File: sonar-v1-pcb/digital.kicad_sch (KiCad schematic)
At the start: 28 parts, among them J40 DIP-48 socket - Cmod A7-35T, J41 FT232H breakout header (Adafr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, J42 PDM array header / Pico 2 rib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, J43 HR911105A MagJack, J44 SJ1 DNP: Cmod 3V3 <> board +3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, J45 SJ2 DNP: Cmod VU <> board 5V, U50 LAN8720A, X1 50 MHz (DNP)

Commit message: T-011 audit: PASS all areas; fix LAN8720A refdes U50->U60 collision; regenerate sheet/pinmap/XDC
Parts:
- removed U50: LAN8720A, Package_DFN_QFN:QFN-24-1EP_4x4mm_P0.5mm_EP2.5x2.5mm, symbol Interface_Ethernet:LAN8720A
- added U60: LAN8720A, Package_DFN_QFN:QFN-24-1EP_4x4mm_P0.5mm_EP2.5x2.5mm, symbol Interface_Ethernet:LAN8720A
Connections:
- net +3.3V: now also U60.1 (VDD2A), U60.19 (VDD1A), U60.9 (VDDIO)
- net ETH_CRS_DV: now also U60.11 (CRS_DV/MODE2)
- net ETH_INTSEL: now also U60.2 (LED2/~{INTSEL})
- net ETH_MDC: now also U60.13 (MDC)
- net ETH_MDIO: now also U60.12 (MDIO)
- net ETH_RBIAS: now also U60.24 (RBIAS)
- net ETH_REF_CLK: now also U60.5 (XTAL1/CLKIN)
- net ETH_REGOFF: now also U60.3 (LED1/REGOFF)
- net ETH_RST_N: now also U60.15 (~{RST})
- net ETH_RXD0: now also U60.8 (RXD0/MODE0)
- net ETH_RXD1: now also U60.7 (RXD1/MODE1)
- net ETH_RXN: now also U60.22 (RXN)
- net ETH_RXP: now also U60.23 (RXP)
- net ETH_RX_ER: now also U60.10 (RXER/PHYAD0)
- net ETH_TXD0: now also U60.17 (TXD0)
- net ETH_TXD1: now also U60.18 (TXD1)
- net ETH_TXN: now also U60.20 (TXN)
- net ETH_TXP: now also U60.21 (TXP)
- net ETH_TX_EN: now also U60.16 (TXEN)
- net ETH_VDDCR: now also U60.6 (VDDCR)
- net GND: now also U60.25 (VSS)
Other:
- note added: "AUTHORITATIVE PIN TABLE: orchestration/pinmap.md (generated by scripts/gen_digital_sheet.py). Clock-capable pins: PDM_CLK_FB=pio36 (MRCC), FT_CLKOUT=pio43 (SRCC), ETH_REF_CLK=pio3 (MRCC) - all double-sourced. Package pins: offline transcription of the Digilent Cmod-A7-Master.xdc, audited offline by a second agent 2026-08-26; live master-XDC diff still required before T-020 synthesis (see orchestr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"
- note added: "DNP ETHERNET PROVISION (D012 amendment b): U60 LAN8720A + J43 HR911105A MagJack + X1 50 MHz osc + R400-R403/C400-C406 are ALL DNP on v1. 100M RMII carries only the decimated stream (raw PDM needs the FT232H). Populate-and-learn milestone, never a respin. MODE[2:0]/PHYAD0 strap levels (RXD0/RXD1/CRS_DV/RXER pins) are sampled at nRST release - Artix-7 config-time weak pull-ups can override the PHY'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"
- note removed: "AUTHORITATIVE PIN TABLE: orchestration/pinmap.md (generated by scripts/gen_digital_sheet.py). Clock-capable pins: PDM_CLK_FB=pio36 (MRCC), FT_CLKOUT=pio43 (SRCC), ETH_REF_CLK=pio3 (MRCC) - all double-sourced. Package pins are offline transcriptions of the Digilent Cmod-A7-Master.xdc - audit against the live master XDC before T-020 synthesis."
- note removed: "DNP ETHERNET PROVISION (D012 amendment b): U50 LAN8720A + J43 HR911105A MagJack + X1 50 MHz osc + R400-R403/C400-C406 are ALL DNP on v1. 100M RMII carries only the decimated stream (raw PDM needs the FT232H). Populate-and-learn milestone, never a respin. MODE[2:0]/PHYAD0 strap levels (RXD0/RXD1/CRS_DV/RXER pins) are sampled at nRST release - Artix-7 config-time weak pull-ups can override the PHY'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"
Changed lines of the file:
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@@
 		)
 	)
-	(text "AUTHORITATIVE PIN TABLE: orchestration/pinmap.md (generated by scripts/gen_digital_sheet.py).\nClock-capable pins: PDM_CLK_FB=pio36 (MRCC), FT_CLKOUT=pio43 (SRCC), ETH_REF_CLK=pio3 (MRCC) - all double-sourced.\nPackage pins are offline transcriptions of the Digilent Cmod-A7-Master.xdc - audit against the live master XDC before T-020 synthesis."
+	(text "AUTHORITATIVE PIN TABLE: orchestration/pinmap.md (generated by scripts/gen_digital_sheet.py).\nClock-capable pins: PDM_CLK_FB=pio36 (MRCC), FT_CLKOUT=pio43 (SRCC), ETH_REF_CLK=pio3 (MRCC) - all double-sourced.\nPackage pins: offline transcription of the Digilent Cmod-A7-Master.xdc, audited offline by a second agent 2026-08-26;\nlive master-XDC diff still required before T-020 synthesis (see orchestration/pinmap.md)."
 		(exclude_from_sim no)
 		(at 25.4 18.5 0)
@@
 		)
 	)
-	(text "DNP ETHERNET PROVISION (D012 amendment b): U50 LAN8720A + J43 HR911105A MagJack + X1 50 MHz osc + R400-R403/C400-C406 are ALL DNP on v1.\n100M RMII carries only the decimated stream (raw PDM needs the FT232H). Populate-and-learn milestone, never a respin.\nMODE[2:0]/PHYAD0 strap levels (RXD0/RXD1/CRS_DV/RXER pins) are sampled at nRST release - Artix-7 config-time weak pull-ups can\noverride the PHY's internal strap pulls; determine strap resistors from the LAN8720A datasheet at populate time.\nTCT to +3.3V / RCT decoupled per LAN8720A voltage-mode reference - verify against the chosen PHY+jack datasheets at populate."
+	(text "DNP ETHERNET PROVISION (D012 amendment b): U60 LAN8720A + J43 HR911105A MagJack + X1 50 MHz osc + R400-R403/C400-C406 are ALL DNP on v1.\n100M RMII carries only the decimated stream (raw PDM needs the FT232H). Populate-and-learn milestone, never a respin.\nMODE[2:0]/PHYAD0 strap levels (RXD0/RXD1/CRS_DV/RXER pins) are sampled at nRST release - Artix-7 config-time weak pull-ups can\noverride the PHY's internal strap pulls; determine strap resistors from the LAN8720A datasheet at populate time.\nTCT to +3.3V / RCT decoupled per LAN8720A voltage-mode reference - verify against the chosen PHY+jack datasheets at populate."
 		(exclude_from_sim no)
 		(at 285 25 0)
@@
 		(dnp yes)
 		(fields_autoplaced yes)
-		(property "Reference" "U50"
+		(property "Reference" "U60"
 			(at 340.36 111.76 0)
 			(show_name no)
@@
 			(project "sonar"
 				(path "/f72ceae0-eee4-4385-b0e8-639846bcb5f2/d19a7a11-b1c2-4d3e-8f40-a11d1a11ce11"
-					(reference "U50")
+					(reference "U60")
 					(unit 1)
 				)

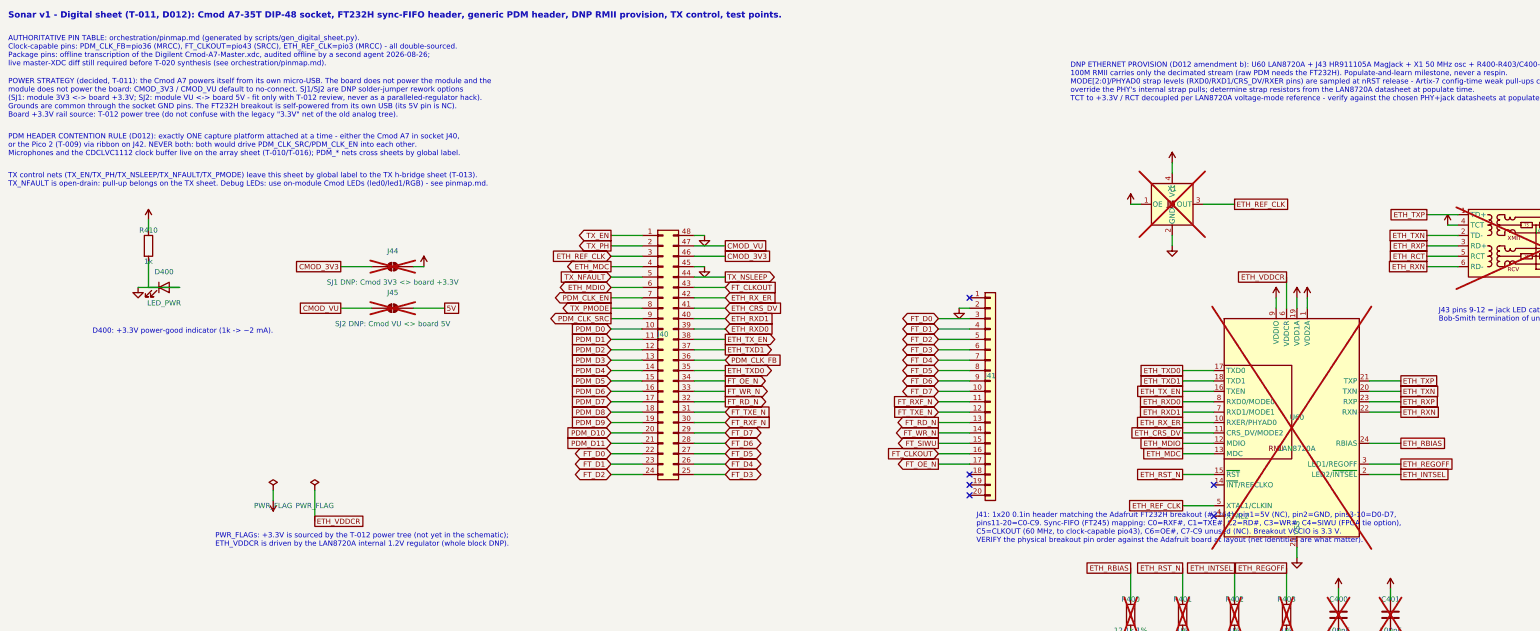
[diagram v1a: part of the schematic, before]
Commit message: T-011 repair: true DIP positions (skip 15/16 analog, 24=VU 25=GND); live-XDC check script; revert CC list to true labels
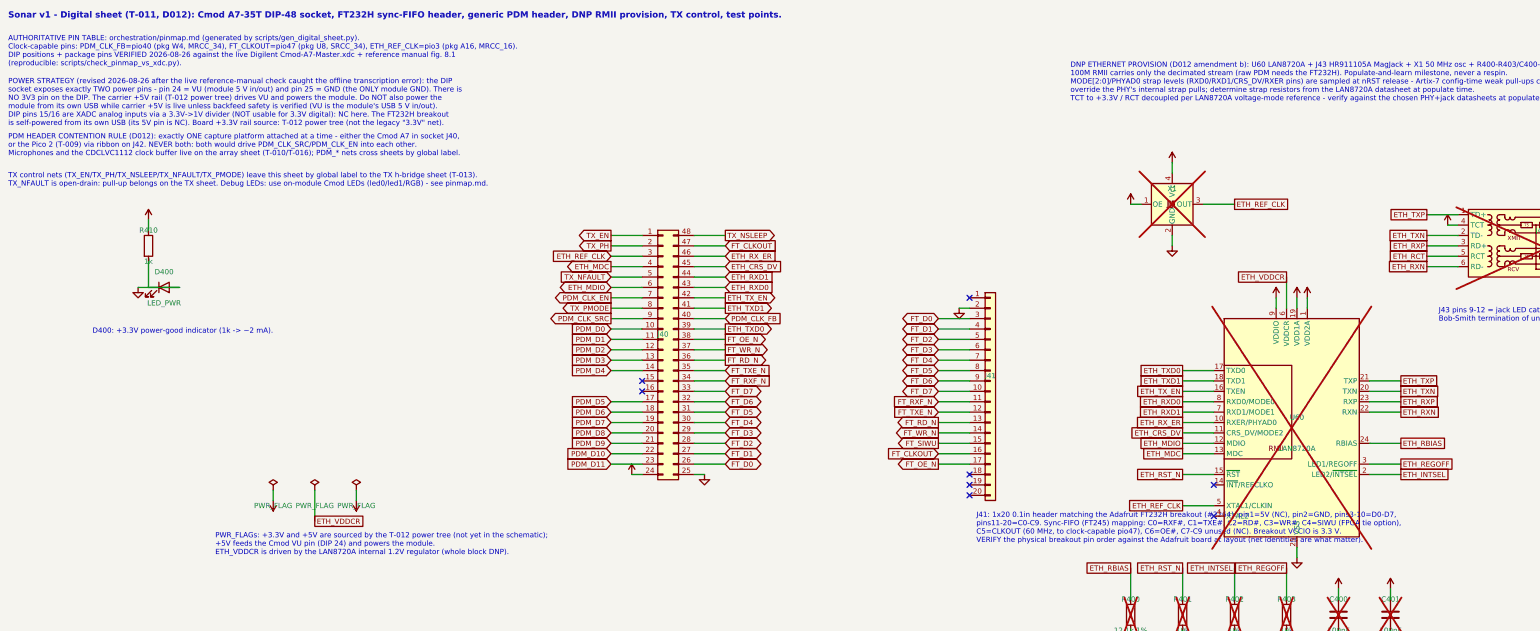
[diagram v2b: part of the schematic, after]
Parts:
- removed J44: SJ1 DNP: Cmod 3V3 <> board +3.3V, Jumper:SolderJumper-2_P1.3mm_Open_RoundedPad1.0x1.5mm, symbol Jumper:SolderJumper_2_Open
- removed J45: SJ2 DNP: Cmod VU <> board 5V, Jumper:SolderJumper-2_P1.3mm_Open_RoundedPad1.0x1.5mm, symbol Jumper:SolderJumper_2_Open
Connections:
- net CMOD_3V3 is gone; now on net ETH_RX_ER: J40.46 (Pin_46)
- net CMOD_VU is gone; now on net FT_CLKOUT: J40.47 (Pin_47)
- net ETH_CRS_DV: now also J40.45 (Pin_45); no longer J40.41 (Pin_41)
- net ETH_RXD0: now also J40.43 (Pin_43); no longer J40.39 (Pin_39)
- net ETH_RXD1: now also J40.44 (Pin_44); no longer J40.40 (Pin_40)
- net ETH_RX_ER: no longer J40.42 (Pin_42)
- net ETH_TXD0: now also J40.39 (Pin_39); no longer J40.35 (Pin_35)
- net ETH_TXD1: now also J40.41 (Pin_41); no longer J40.37 (Pin_37)
- net ETH_TX_EN: now also J40.42 (Pin_42); no longer J40.38 (Pin_38)
- net FT_CLKOUT: no longer J40.43 (Pin_43)
- net FT_D0: now also J40.26 (Pin_26); no longer J40.22 (Pin_22)
- net FT_D1: now also J40.27 (Pin_27); no longer J40.23 (Pin_23)
- net FT_D2: now also J40.28 (Pin_28); no longer J40.24 (Pin_24)
- net FT_D3: now also J40.29 (Pin_29); no longer J40.25 (Pin_25)
- net FT_D4: now also J40.30 (Pin_30); no longer J40.26 (Pin_26)
- net FT_D5: now also J40.31 (Pin_31); no longer J40.27 (Pin_27)
- net FT_D6: now also J40.32 (Pin_32); no longer J40.28 (Pin_28)
- net FT_D7: now also J40.33 (Pin_33); no longer J40.29 (Pin_29)
- net FT_OE_N: now also J40.38 (Pin_38); no longer J40.34 (Pin_34)
- net FT_RD_N: now also J40.36 (Pin_36); no longer J40.32 (Pin_32)
- net FT_RXF_N: now also J40.34 (Pin_34); no longer J40.30 (Pin_30)
- net FT_TXE_N: now also J40.35 (Pin_35); no longer J40.31 (Pin_31)
- net FT_WR_N: now also J40.37 (Pin_37); no longer J40.33 (Pin_33)
- net GND: now also J40.25 (Pin_25); no longer J40.45 (Pin_45), J40.48 (Pin_48)
- net PDM_CLK_FB: now also J40.40 (Pin_40); no longer J40.36 (Pin_36)
- net PDM_D10: now also J40.22 (Pin_22); no longer J40.20 (Pin_20)
- net PDM_D11: now also J40.23 (Pin_23); no longer J40.21 (Pin_21)
- net PDM_D5: now also J40.17 (Pin_17); no longer J40.15 (Pin_15)
- net PDM_D6: now also J40.18 (Pin_18); no longer J40.16 (Pin_16)
- net PDM_D7: now also J40.19 (Pin_19); no longer J40.17 (Pin_17)
- net PDM_D8: now also J40.20 (Pin_20); no longer J40.18 (Pin_18)
- net PDM_D9: now also J40.21 (Pin_21); no longer J40.19 (Pin_19)
- net TX_NSLEEP: now also J40.48 (Pin_48); no longer J40.44 (Pin_44)
- new net +5V: J40.24 (Pin_24)
- no-connect marks 10 -> 12
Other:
- note added: "AUTHORITATIVE PIN TABLE: orchestration/pinmap.md (generated by scripts/gen_digital_sheet.py). Clock-capable pins: PDM_CLK_FB=pio40 (pkg W4, MRCC_34), FT_CLKOUT=pio47 (pkg U8, SRCC_34), ETH_REF_CLK=pio3 (pkg A16, MRCC_16). DIP positions + package pins VERIFIED 2026-08-26 against the live Digilent Cmod-A7-Master.xdc + reference manual fig. 8.1 (reproducible: scripts/check_pinmap_vs_xdc.py)."
- note added: "J41: 1x20 0.1in header matching the Adafruit FT232H breakout (#2264): pin1=5V (NC), pin2=GND, pins3-10=D0-D7, pins11-20=C0-C9. Sync-FIFO (FT245) mapping: C0=RXF#, C1=TXE#, C2=RD#, C3=WR#, C4=SIWU (FPGA tie option), C5=CLKOUT (60 MHz, to clock-capable pio47), C6=OE#, C7-C9 unused (NC). Breakout VCCIO is 3.3 V. VERIFY the physical breakout pin order against the Adafruit board at layout (net identit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"
- note added: "POWER STRATEGY (revised 2026-08-26 after the live reference-manual check caught the offline transcription error): the DIP socket exposes exactly TWO power pins - pin 24 = VU (module 5 V in/out) and pin 25 = GND (the ONLY module GND). There is NO 3V3 pin on the DIP. The carrier +5V rail (T-012 power tree) drives VU and powers the module. Do NOT also power the module from its own USB while carrier 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"
- note added: "PWR_FLAGs: +3.3V and +5V are sourced by the T-012 power tree (not yet in the schematic); +5V feeds the Cmod VU pin (DIP 24) and powers the module. ETH_VDDCR is driven by the LAN8720A internal 1.2V regulator (whole block DNP)."
- note removed: "AUTHORITATIVE PIN TABLE: orchestration/pinmap.md (generated by scripts/gen_digital_sheet.py). Clock-capable pins: PDM_CLK_FB=pio36 (MRCC), FT_CLKOUT=pio43 (SRCC), ETH_REF_CLK=pio3 (MRCC) - all double-sourced. Package pins: offline transcription of the Digilent Cmod-A7-Master.xdc, audited offline by a second agent 2026-08-26; live master-XDC diff still required before T-020 synthesis (see orchestr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"
- note removed: "J41: 1x20 0.1in header matching the Adafruit FT232H breakout (#2264): pin1=5V (NC), pin2=GND, pins3-10=D0-D7, pins11-20=C0-C9. Sync-FIFO (FT245) mapping: C0=RXF#, C1=TXE#, C2=RD#, C3=WR#, C4=SIWU (FPGA tie option), C5=CLKOUT (60 MHz, to clock-capable pio43), C6=OE#, C7-C9 unused (NC). Breakout VCCIO is 3.3 V. VERIFY the physical breakout pin order against the Adafruit board at layout (net identit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"
- note removed: "POWER STRATEGY (decided, T-011): the Cmod A7 powers itself from its own micro-USB. The board does not power the module and the module does not power the board: CMOD_3V3 / CMOD_VU default to no-connect. SJ1/SJ2 are DNP solder-jumper rework options (SJ1: module 3V3 <-> board +3.3V; SJ2: module VU <-> board 5V - fit only with T-012 review, never as a paralleled-regulator hack). Grounds are common th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"
- note removed: "PWR_FLAGs: +3.3V is sourced by the T-012 power tree (not yet in the schematic); ETH_VDDCR is driven by the LAN8720A internal 1.2V regulator (whole block DNP)."

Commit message: review fixes B1/S1/S2/S9: unify Cmod VU on 5V rail + DNP-able 0R feed, XDC regen preserves MANUAL APPEND, rails.md power strategy + Cmod budget, FT_SIWU pull-up
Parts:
- added R411: 10k, Resistor_SMD:R_0603_1608Metric, symbol Device:R
- added R420: 0R, Resistor_SMD:R_0603_1608Metric, symbol Device:R
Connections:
- net +3.3V: now also R411.1
- net FT_SIWU: now also R411.2
- net +5V renamed 5V_CMOD
- net 5V_CMOD: now also R420.1
- new net 5V: R420.2
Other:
- note added: "POWER STRATEGY (revised 2026-08-26; review-B1 fix): the DIP socket exposes exactly TWO power pins - pin 24 = VU (module 5 V in/out) and pin 25 = GND (the ONLY module GND). There is NO 3V3 pin on the DIP. The carrier 5V rail (T-012 power tree, global net "5V") powers the module through R420 (0R 0603, populated by default) -> 5V_CMOD -> J40 pin 24. Backfeed caveat: VU is the module's own USB 5 V in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"
- note added: "PWR_FLAGs: +3.3V is sourced by the T-012 power tree (power_supply sheet); the flag is kept so this sheet is ERC-clean standalone. The stale +5V PWR_FLAG that masked the orphan VU net (review 2026-08-26 B1) is DELETED - the VU feed now runs J40.24 -> R420 (0R) -> the global 5V net driven by the power mux. ETH_VDDCR is driven by the LAN8720A internal 1.2V regulator (whole block DNP)."
- note added: "R411: FT_SIWU (SIWU#) pull-up to +3.3V, 10k 0603 - a floating FTDI control input is not a safe default (review S9)."
- note added: "R420: 0R 0603 in the Cmod VU feed (5V -> 5V_CMOD -> J40 pin 24). Populated by default (v1 power strategy: carrier 5V powers the module). DNP to isolate the module from carrier 5V - the backfeed-safe procedure for running the Cmod from its own USB (bitstream load / D012 snapshot drain) while the carrier is live. See orchestration/rails.md. (Review 2026-08-26 B1.)"
- note removed: "POWER STRATEGY (revised 2026-08-26 after the live reference-manual check caught the offline transcription error): the DIP socket exposes exactly TWO power pins - pin 24 = VU (module 5 V in/out) and pin 25 = GND (the ONLY module GND). There is NO 3V3 pin on the DIP. The carrier +5V rail (T-012 power tree) drives VU and powers the module. Do NOT also power the module from its own USB while carrier 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"
- note removed: "PWR_FLAGs: +3.3V and +5V are sourced by the T-012 power tree (not yet in the schematic); +5V feeds the Cmod VU pin (DIP 24) and powers the module. ETH_VDDCR is driven by the LAN8720A internal 1.2V regulator (whole block DNP)."
